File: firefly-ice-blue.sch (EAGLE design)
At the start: 120 parts, among them J1 USB-5PINZX62WD1-B-5PC, J2 CON-6SOCKET, U1 EFM32LG330F256, U10 STM6519, U11 TPS782XX, U12 TPS6208X, U13 NX3L1T53, U14 FDFMA2P029Z, U16 MEMORY-SPIWLBGA-8, U17 ADP151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

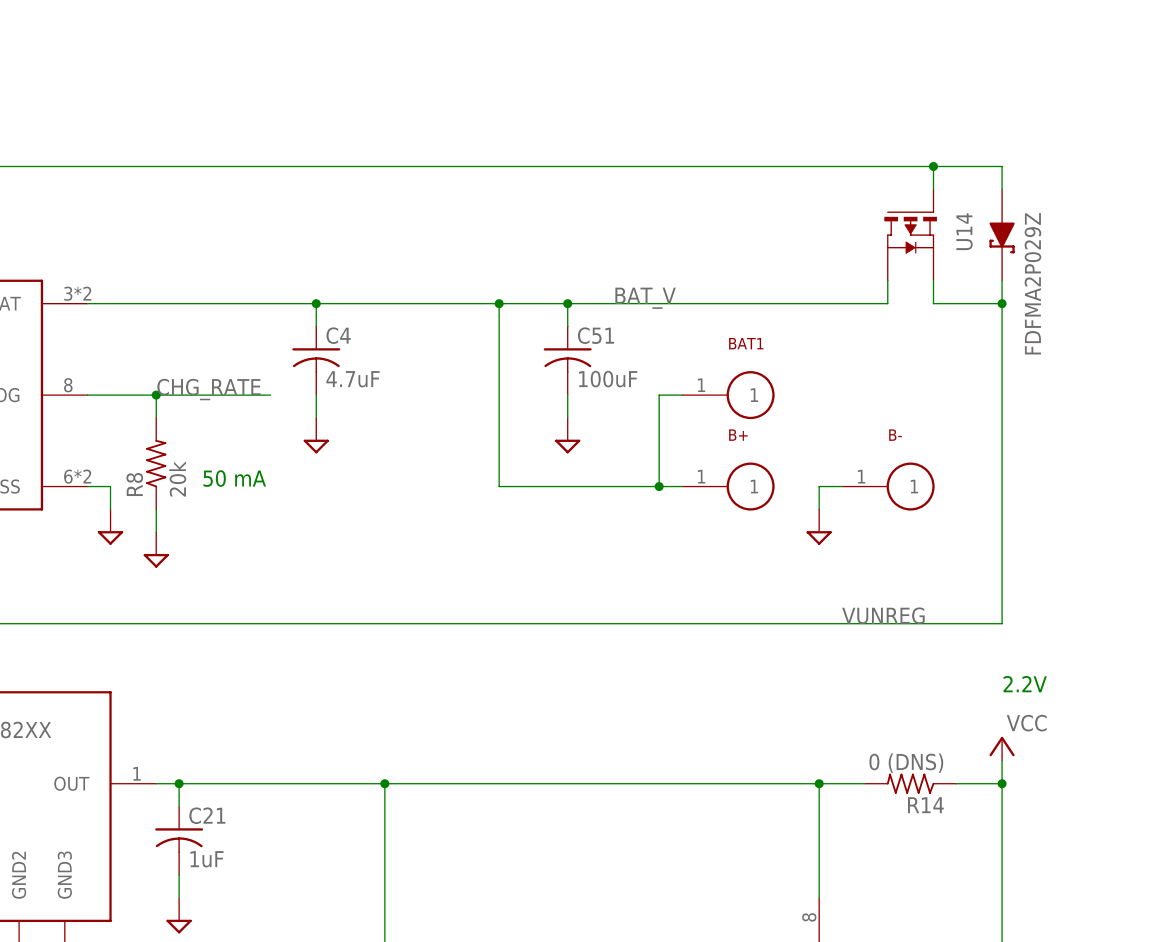
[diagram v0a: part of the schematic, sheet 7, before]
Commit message: add test fixture board
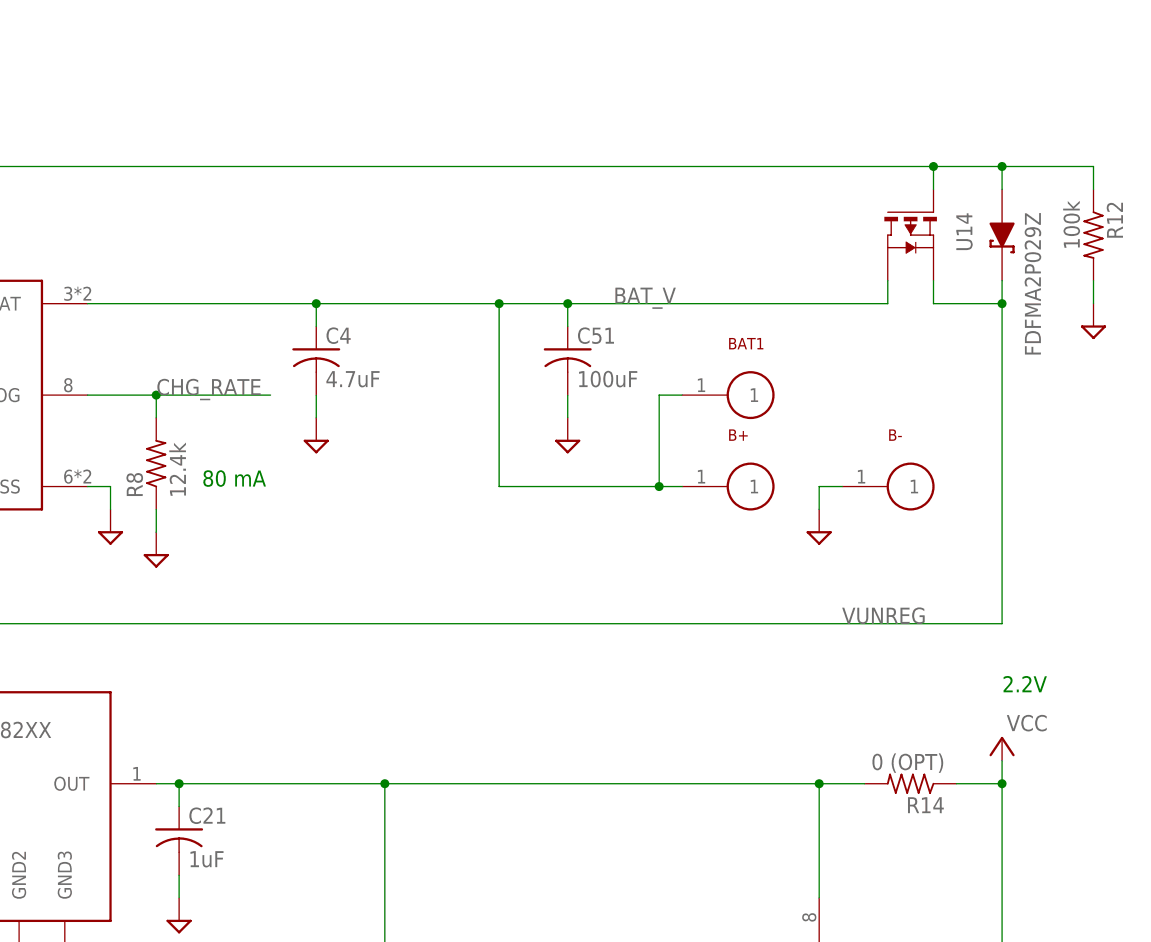
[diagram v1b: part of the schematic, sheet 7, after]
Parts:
- added R12: 100k, firefly:R-US_R0201
- C15, C5: ORDERING-CODE C1005X5R0J475M -> C1005X5R0J475M050BC
- C39: ORDERING-CODE C0603X7R1E102K -> C0603X7R1E102K030BA
- C4: ORDERING-CODE C1005X5R0J475M -> C1005X5R0J475M050BC; VARIANTS (none) -> usb-charging
- C44: ORDERING-CODE C0603X5R1E222K -> C0603X5R1E222K030BA
- C46, C6: ORDERING-CODE C0603C0G1E1R2BTQ -> C0603C0G1E1R2B030BF
- C47: ORDERING-CODE C0603C0G1E1R8CTQ -> C0603C0G1E1R8C030BF
- C53, C54: ORDERING-CODE C0603X5R0J474M -> C0603X5R0J474M030BC
- R14, R5: value 0 (DNS) -> 0 (OPT)
- R31, R32, R33, R7: VARIANTS efficient-power -> (none)
- R6: value 50 -> 25; ORDERING-CODE ERJ-1GEF51R0C -> ERJ-1GEF24R9C
- R8: value 20k -> 12.4k; ORDERING-CODE ERJ-1GEF2002C -> ERJ-1GEF1242C
- U14: DNS (none) -> true; VARIANTS usb-power -> (none)
- U8: VARIANTS (none) -> usb-power
- X1: MANUFACTURER TXC CORPORATION -> AVX Corp/Kyocera Corp; ORDERING-CODE 9HT10-32.768KEZF-T -> ST3215SB32768B0HPWB3
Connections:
- net BAT_V: now also U14.D; no longer U14.S
- net GND: now also R12.2
- net USB_VBUS: now also R12.1
- net VUNREG: now also U14.S; no longer U14.D
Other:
- note added: "80 mA"
- note removed: "50 mA"

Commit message: update some ordering codes
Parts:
- U1: ORDERING-CODE EFM32LG330F256 -> EFM32LG330F256-QFN64
- U16: ORDERING-CODE W25Q16DWBYIG -> W25Q16DWBYIG-TR
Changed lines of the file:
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@@
 <part name="U1" library="firefly" deviceset="EFM32LG330F256" device="">
 <attribute name="MANUFACTURER" value="Energy Micro"/>
-<attribute name="ORDERING-CODE" value="EFM32LG330F256"/>
+<attribute name="ORDERING-CODE" value="EFM32LG330F256-QFN64"/>
 </part>
 <part name="R6" library="firefly" deviceset="R-US_" device="R0201" value="25">
@@
 <attribute name="DISTRIBUTOR" value="Arrow"/>
 <attribute name="MANUFACTURER" value="Winbond"/>
-<attribute name="ORDERING-CODE" value="W25Q16DWBYIG"/>
+<attribute name="ORDERING-CODE" value="W25Q16DWBYIG-TR"/>
 </part>
 <part name="U$3" library="firefly" deviceset="VCC" device=""/>

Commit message: raise voltage to 2.5V; make external usb id reset optional
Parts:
- removed USBID: TARGET-PIN, firefly:TARGET-PIN
- added EXTRESET: TARGET-PIN, firefly:TARGET-PIN
- added R13: 0 (OPT), firefly:R-US_R0201
- R3: value 152.4k -> 182k; ORDERING-CODE ERJ-1GEF1503C -> ERJ-1GEF1823C
- U11: ORDERING-CODE TPS78222DRVR -> TPS78225DRVR
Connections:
- new net N$14: EXTRESET.1, R13.2, R2.2, U10.!SR
- net N$8: now also R13.1; no longer R2.2, U10.!SR, USBID.1
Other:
- note added: "2.5V"
- note removed: "2.2V"
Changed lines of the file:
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@@
 <part name="U11" library="firefly" deviceset="TPS782XX" device="">
 <attribute name="MANUFACTURER" value="Texas Instruments"/>
-<attribute name="ORDERING-CODE" value="TPS78222DRVR"/>
+<attribute name="ORDERING-CODE" value="TPS78225DRVR"/>
 </part>
 <part name="U12" library="firefly" deviceset="TPS6208X" device="">
@@
 <attribute name="VARIANTS" value="efficient-power"/>
 </part>
-<part name="R3" library="firefly" deviceset="R-US_" device="R0201" value="152.4k">
+<part name="R3" library="firefly" deviceset="R-US_" device="R0201" value="182k">
 <attribute name="MANUFACTURER" value="Panasonic Electronic Components"/>
-<attribute name="ORDERING-CODE" value="ERJ-1GEF1503C"/>
+<attribute name="ORDERING-CODE" value="ERJ-1GEF1823C"/>
 <attribute name="VARIANTS" value="efficient-power"/>
 </part>
@@
 <attribute name="VARIANTS" value="expansion"/>
 </part>
-<part name="USBID" library="firefly" deviceset="TARGET-PIN" device=""/>
+<part name="EXTRESET" library="firefly" deviceset="TARGET-PIN" device=""/>
 <part name="D1" library="firefly" deviceset="LED-RGB" device="">
 <attribute name="MANUFACTURER" value="Rohm Semiconductor"/>
@@
 <attribute name="ORDERING-CODE" value="RC0201FR-07100KL"/>
 </part>
+<part name="R13" library="firefly" deviceset="R-US_" device="R0201" value="0 (OPT)">
+<attribute name="MANUFACTURER" value="Panasonic Electronic Components"/>
+<attribute name="ORDERING-CODE" value="ERJ-1GE0R00C"/>
+<attribute name="VARIANTS" value="!usb-id-failsafe"/>
+</part>
 </parts>
 <sheets>
@@
 <sheet>
 <plain>
-<text x="256.54" y="132.08" size="1.778" layer="91">2.2V</text>
+<text x="256.54" y="132.08" size="1.778" layer="91">2.5V</text>
 <text x="167.64" y="154.94" size="1.778" layer="91">80 mA</text>
 </plain>
@@
 </instance>
 <instance part="V55" gate="GND" x="210.82" y="71.12"/>
-<instance part="USBID" gate="G$1" x="27.94" y="200.66" rot="R90"/>
+<instance part="EXTRESET" gate="G$1" x="20.32" y="124.46" rot="R90"/>
 <instance part="U14" gate="G$1" x="251.46" y="182.88" rot="R270">
 <attribute name="DNS" x="251.46" y="182.88" size="1.778" layer="96" rot="R270" display="off"/>
@@
 <attribute name="DNS" x="266.7" y="182.88" size="1.778" layer="96" rot="R270" display="off"/>
 </instance>
+<instance part="R13" gate="G$1" x="30.48" y="121.92" rot="R270">
+<attribute name="VARIANTS" x="30.48" y="121.92" size="1.778" layer="96" rot="R270" display="off"/>
+<attribute name="MANUFACTURER" x="30.48" y="121.92" size="1.778" layer="96" rot="R270" display="off"/>
+<attribute name="ORDERING-CODE" x="30.48" y="121.92" size="1.778" layer="96" rot="R270" display="off"/>
+</instance>
 </instances>
 <busses>
@@
 <net name="N$8" class="0">
 <segment>
-<wire x1="40.64" y1="114.3" x2="33.02" y2="114.3" width="0.1524" layer="91"/>
-<wire x1="40.64" y1="116.84" x2="40.64" y2="114.3" width="0.1524" layer="91"/>
-<wire x1="33.02" y1="114.3" x2="33.02" y2="182.88" width="0.1524" layer="91"/>
 <pinref part="J1" gate="G$1" pin="ID"/>
-<wire x1="33.02" y1="182.88" x2="27.94" y2="182.88" width="0.1524" layer="91"/>
-<pinref part="R2" gate="G$1" pin="2"/>
+<wire x1="33.02" y1="182.88" x2="30.48" y2="182.88" width="0.1524" layer="91"/>
+<wire x1="30.48" y1="182.88" x2="27.94" y2="182.88" width="0.1524" layer="91"/>
 <wire x1="27.94" y1="182.88" x2="22.86" y2="182.88" width="0.1524" layer="91"/>
-<wire x1="43.18" y1="114.3" x2="40.64" y2="114.3" width="0.1524" layer="91"/>
-<junction x="40.64" y="114.3"/>
-<pinref part="U10" gate="G$1" pin="!SR"/>
 <pinref part="U8" gate="G$1" pin="IO1"/>
 <wire x1="33.02" y1="182.88" x2="38.1" y2="182.88" width="0.1524" layer="91"/>
 <wire x1="38.1" y1="182.88" x2="38.1" y2="175.26" width="0.1524" layer="91"/>
-<junction x="33.02" y="182.88"/>
-<pinref part="USBID" gate="G$1" pin="1"/>
-<wire x1="27.94" y1="193.04" x2="27.94" y2="182.88" width="0.1524" layer="91"/>
-<junction x="27.94" y="182.88"/>
+<pinref part="R13" gate="G$1" pin="1"/>
+<wire x1="30.48" y1="127" x2="30.48" y2="182.88" width="0.1524" layer="91"/>
+<junction x="30.48" y="182.88"/>
+</segment>
+</net>
+<net name="N$14" class="0">
+<segment>
+<pinref part="R2" gate="G$1" pin="2"/>
+<wire x1="40.64" y1="116.84" x2="40.64" y2="114.3" width="0.1524" layer="91"/>
+<pinref part="U10" gate="G$1" pin="!SR"/>
+<wire x1="43.18" y1="114.3" x2="40.64" y2="114.3" width="0.1524" layer="91"/>
+<junction x="40.64" y="114.3"/>
+<wire x1="40.64" y1="114.3" x2="30.48" y2="114.3" width="0.1524" layer="91"/>
+<pinref part="R13" gate="G$1" pin="2"/>
+<wire x1="30.48" y1="114.3" x2="20.32" y2="114.3" width="0.1524" layer="91"/>
+<wire x1="30.48" y1="116.84" x2="30.48" y2="114.3" width="0.1524" layer="91"/>
+<pinref part="EXTRESET" gate="G$1" pin="1"/>
+<wire x1="20.32" y1="116.84" x2="20.32" y2="114.3" width="0.1524" layer="91"/>
+<junction x="30.48" y="114.3"/>
 </segment>
 </net>

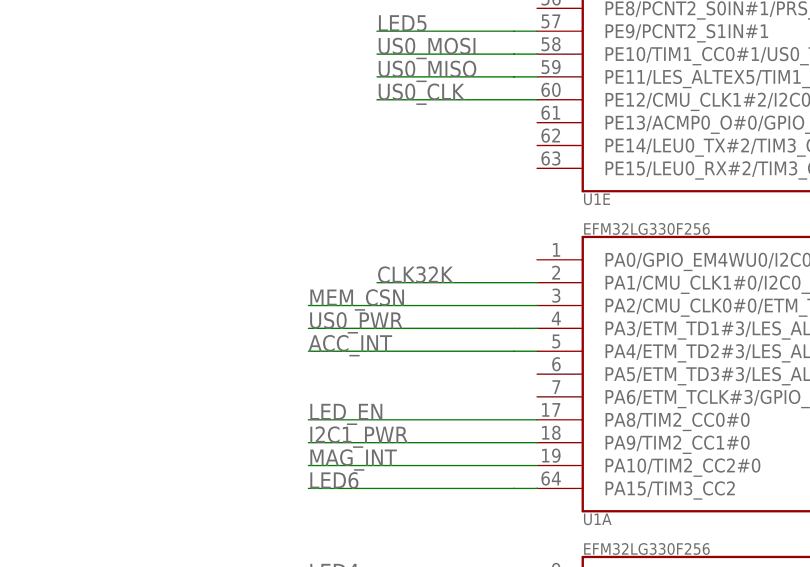
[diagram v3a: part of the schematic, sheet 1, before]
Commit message: add accelerometer interrupt to pin 5 (since pin 4 can't be shared due to radio use)
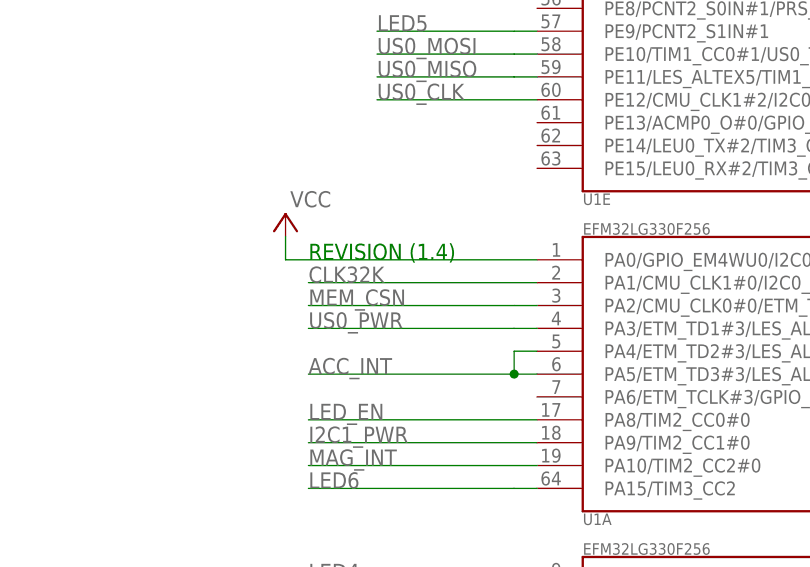
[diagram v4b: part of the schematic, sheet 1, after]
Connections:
- net ACC_INT: now also U1A.PA5/ETM_TD3#3/LES_ALTEX4/LEU1_TX#1/TIM0_CDTI2#0
- net VCC: now also U1A.PA0/GPIO_EM4WU0/I2C0_SDA#0/LEU0_RX#4/PRS_CH0/TIM0_CC0#0,1,4
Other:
- note added: "REVISION (1.4)"
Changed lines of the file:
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@@
 <attribute name="VARIANTS" value="!usb-id-failsafe"/>
 </part>
+<part name="U$9" library="firefly" deviceset="VCC" device=""/>
 </parts>
 <sheets>
 <sheet>
 <plain>
+<text x="43.18" y="289.56" size="1.778" layer="91">REVISION (1.4)</text>
 </plain>
 <instances>
@@
 </instance>
 <instance part="FRAME3" gate="G$1" x="0" y="0"/>
+<instance part="U$9" gate="G$1" x="40.64" y="292.1"/>
 </instances>
 <busses>
@@
 <pinref part="R25" gate="G$1" pin="2"/>
 <wire x1="175.26" y1="147.32" x2="175.26" y2="144.78" width="0.1524" layer="91"/>
+</segment>
+<segment>
+<pinref part="U$9" gate="G$1" pin="VCC"/>
+<wire x1="40.64" y1="292.1" x2="40.64" y2="289.56" width="0.1524" layer="91"/>
+<pinref part="U1" gate="A" pin="PA0/GPIO_EM4WU0/I2C0_SDA#0/LEU0_RX#4/PRS_CH0/TIM0_CC0#0,1,4"/>
+<wire x1="40.64" y1="289.56" x2="68.58" y2="289.56" width="0.1524" layer="91"/>
 </segment>
 </net>
@@
 <net name="ACC_INT" class="0">
 <segment>
-<wire x1="66.04" y1="279.4" x2="43.18" y2="279.4" width="0.1524" layer="91"/>
-<label x="43.18" y="279.4" size="1.778" layer="95"/>
+<wire x1="66.04" y1="276.86" x2="43.18" y2="276.86" width="0.1524" layer="91"/>
+<label x="43.18" y="276.86" size="1.778" layer="95"/>
+<pinref part="U1" gate="A" pin="PA5/ETM_TD3#3/LES_ALTEX4/LEU1_TX#1/TIM0_CDTI2#0"/>
+<wire x1="66.04" y1="276.86" x2="68.58" y2="276.86" width="0.1524" layer="91"/>
 <pinref part="U1" gate="A" pin="PA4/ETM_TD2#3/LES_ALTEX3/TIM0_CDTI1#0"/>
-<wire x1="66.04" y1="279.4" x2="68.58" y2="279.4" width="0.1524" layer="91"/>
+<wire x1="68.58" y1="279.4" x2="66.04" y2="279.4" width="0.1524" layer="91"/>
+<wire x1="66.04" y1="279.4" x2="66.04" y2="276.86" width="0.1524" layer="91"/>
+<junction x="66.04" y="276.86"/>
 </segment>
 </net>
@@
 <segment>
 <pinref part="U1" gate="A" pin="PA1/CMU_CLK1#0/I2C0_SCL#0/PRS_CH1/TIM0_CC1#0,1"/>
-<wire x1="68.58" y1="287.02" x2="50.8" y2="287.02" width="0.1524" layer="91"/>
-<label x="50.8" y="287.02" size="1.778" layer="95"/>
-</segment>
-</net>
+<wire x1="68.58" y1="287.02" x2="43.18" y2="287.02" width="0.1524" layer="91"/>
+<label x="43.18" y="287.02" size="1.778" layer="95"/>
+</segment>
+</net>

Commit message: switch connector
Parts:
- J1: MANUFACTURER Hirose Electric Co Ltd -> TE Connectivity; ORDERING-CODE ZX62WD1-B-5PC -> 2173157-3
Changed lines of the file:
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@@
 </part>
 <part name="J1" library="firefly" deviceset="USB-5PIN" device="ZX62WD1-B-5PC" value="USB-5PINZX62WD1-B-5PC">
-<attribute name="MANUFACTURER" value="Hirose Electric Co Ltd"/>
-<attribute name="ORDERING-CODE" value="ZX62WD1-B-5PC"/>
+<attribute name="MANUFACTURER" value="TE Connectivity"/>
+<attribute name="ORDERING-CODE" value="2173157-3"/>
 <attribute name="VARIANTS" value="usb-power"/>
 </part>
